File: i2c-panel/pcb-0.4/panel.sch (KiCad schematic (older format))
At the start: 23 parts, among them IC1 ATMEGA168-20PU, P1 CONN_6, P2 I2C, P7 CONN_2, SW1 PUSHPUTTON, SW2 PUSHPUTTON, SW3 PUSHPUTTON, SW4 PUSHPUTTON, SW5 JOYSTICK, T1 BC547C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

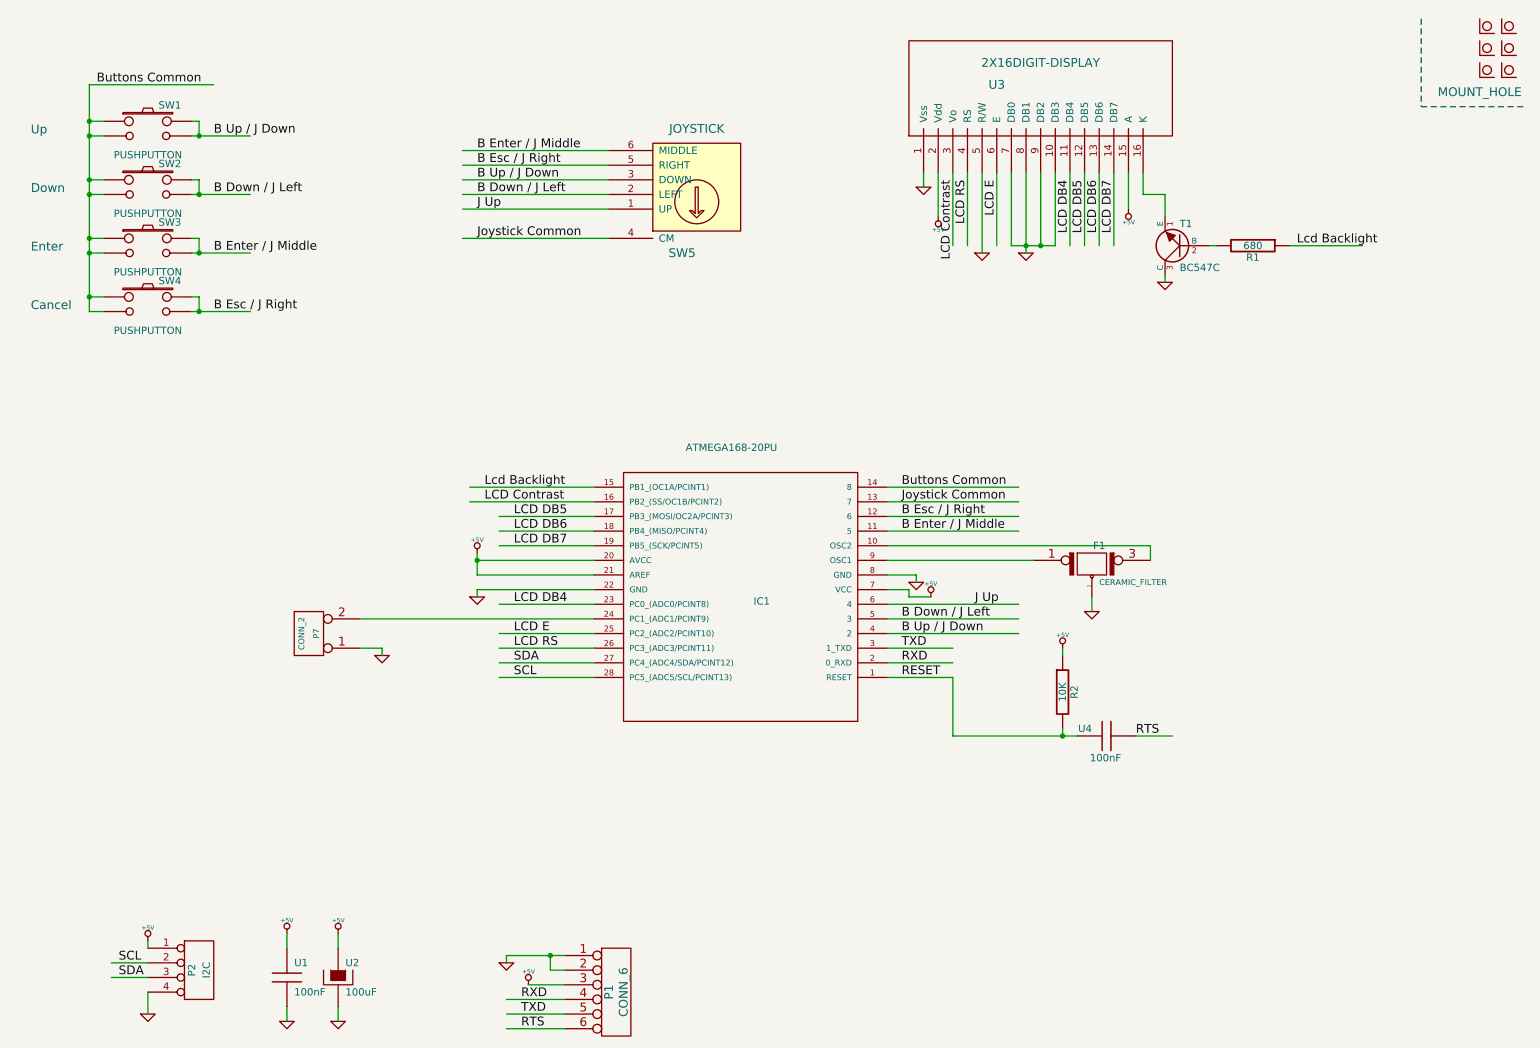
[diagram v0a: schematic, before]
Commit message: I2C level converter, FET for buzzer and ISP connector added
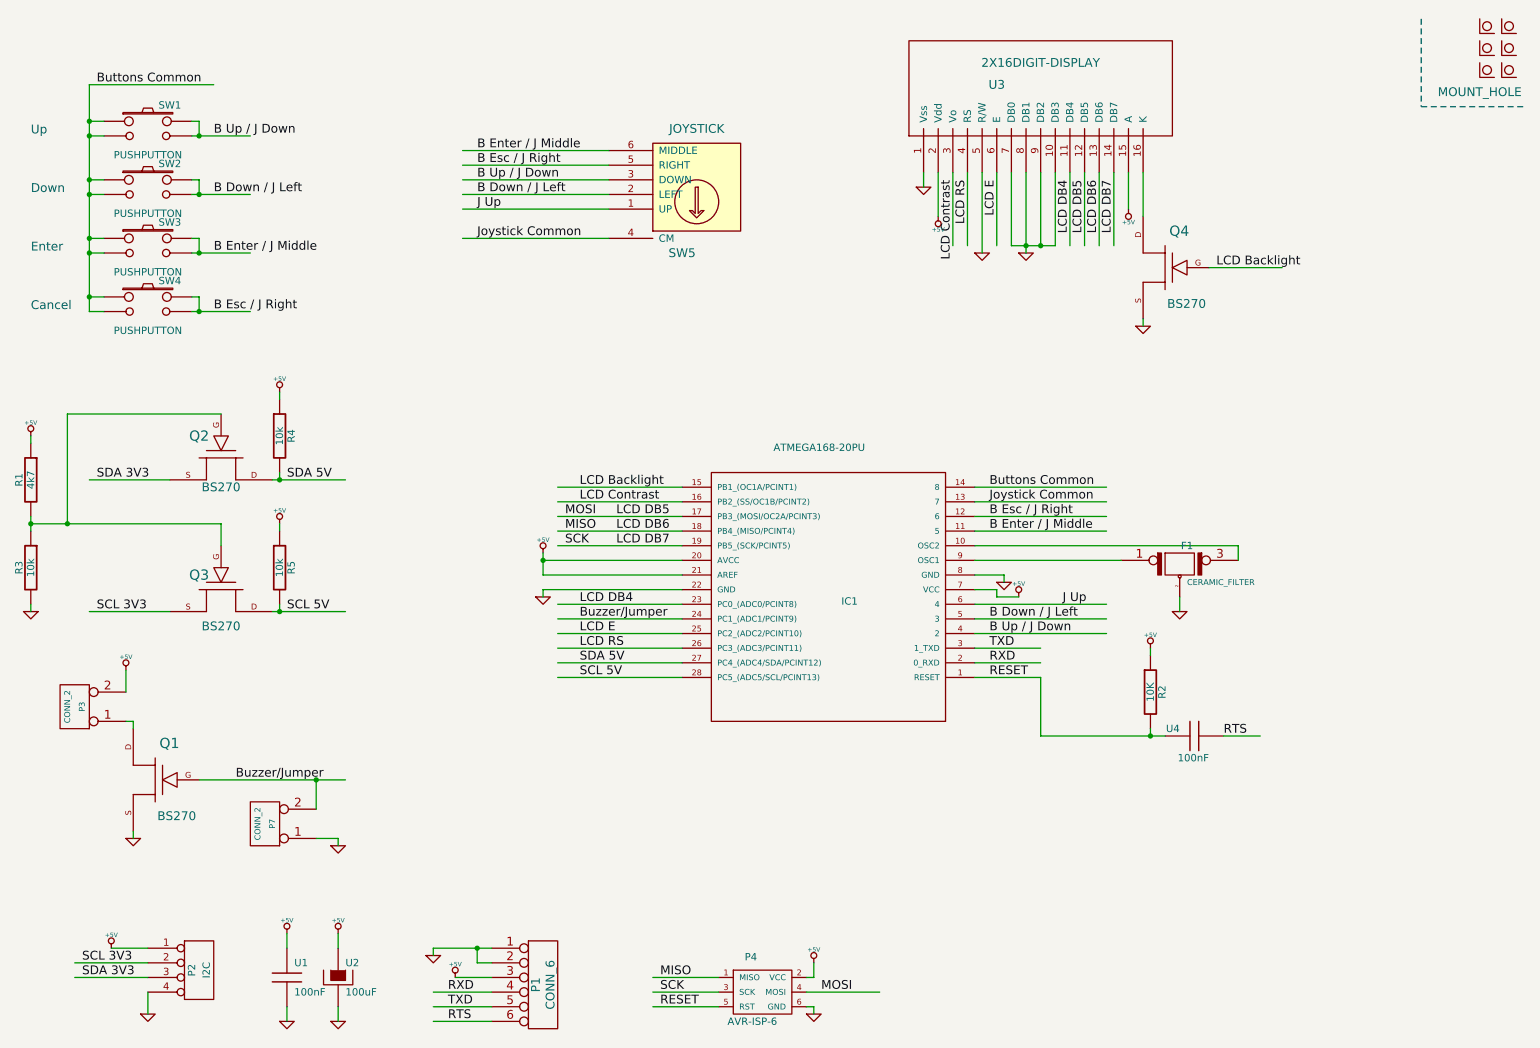
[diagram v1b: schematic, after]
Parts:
- removed T1: BC547C, symbol NPN
- added P3: CONN_2, SIL-1, symbol CONN_2
- added P4: AVR-ISP-6, SIL-1, symbol AVR-ISP-6
- added Q1, Q2, Q3, Q4: BS270, TO92DGS, symbol FET_N
- added R3, R4, R5: 10k, R4, symbol R
- F1: footprint (none) -> SIL-3
- H1, H2, H3, H4, H5, H6: footprint (none) -> HOLE_3MM
- IC1: footprint MLF44 -> DIP-28__300_ELL
- P1: footprint (none) -> SIL-6
- P2: footprint (none) -> SIL-4
- P7: footprint (none) -> SIL-2
- R1: value 680 -> 4k7; footprint (none) -> R4
- R2: footprint (none) -> R4
- SW1, SW2, SW3, SW4: footprint (none) -> PUSHBUTTON
- SW5: footprint (none) -> JOYSTICK_FLIPPED_RIGHT
- U1, U4: footprint (none) -> C2
- U2: footprint (none) -> CCAP_3.5MM
- U3: footprint (none) -> SIL-16
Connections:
- net labels added: Buzzer/Jumper, LCD Backlight, MISO, MOSI, SCK, SCL 3V3, SCL 5V, SDA 3V3, SDA 5V
- net labels removed: Lcd Backlight, SCL, SDA
- wire segments 108 -> 134
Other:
- moved on the sheet: F1, IC1, P1, P7, R2, U4

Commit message: I2C level shifter: not neccesary, pcb enlarged for extra mounting holes
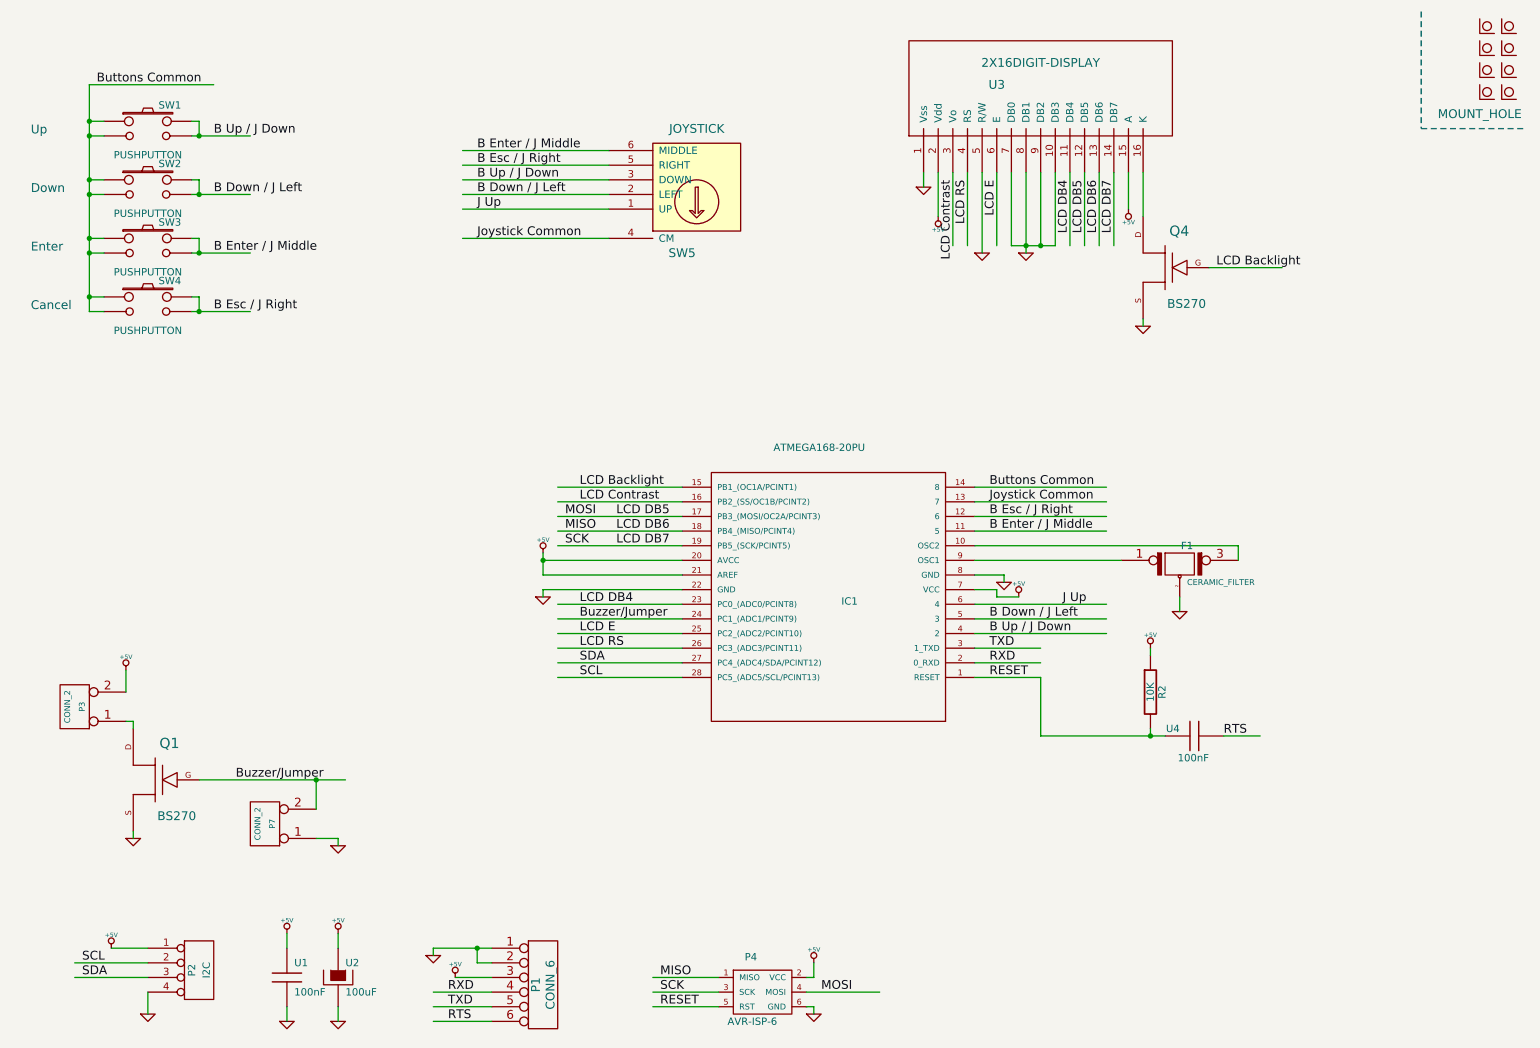
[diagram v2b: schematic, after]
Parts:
- removed Q2, Q3: BS270, TO92DGS, symbol FET_N
- removed R1: 4k7, R4, symbol R
- removed R3, R4, R5: 10k, R4, symbol R
- added H7, H8: MOUNT_HOLE, HOLE_3MM, symbol MOUNT_HOLE
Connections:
- net labels added: SCL, SDA
- net labels removed: SCL 3V3, SCL 5V, SDA 3V3, SDA 5V
- wire segments 134 -> 119

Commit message: Larger holes for pinheaders, extra connector for buzzer
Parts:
- added P5: CONN_4, SIL-4, symbol CONN_4
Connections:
- wire segments 119 -> 124

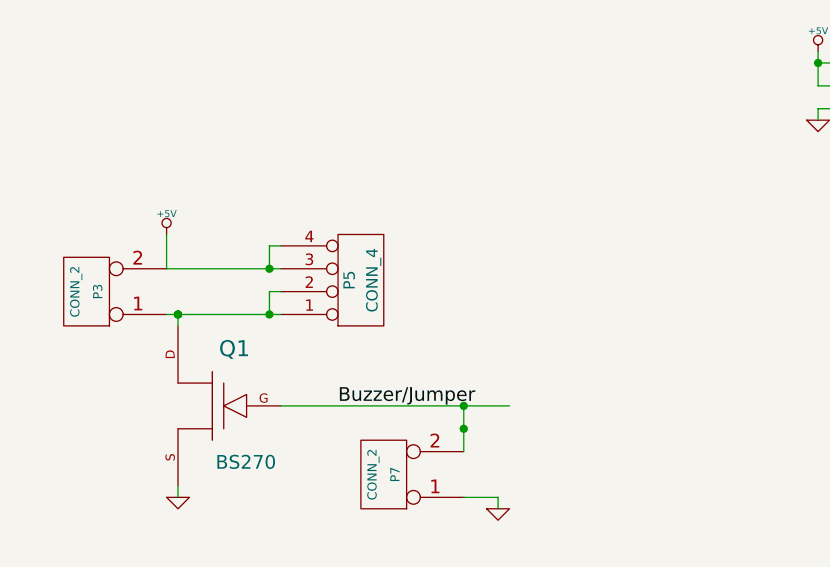
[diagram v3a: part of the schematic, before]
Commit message: Kingstate KPEG242 buzzer
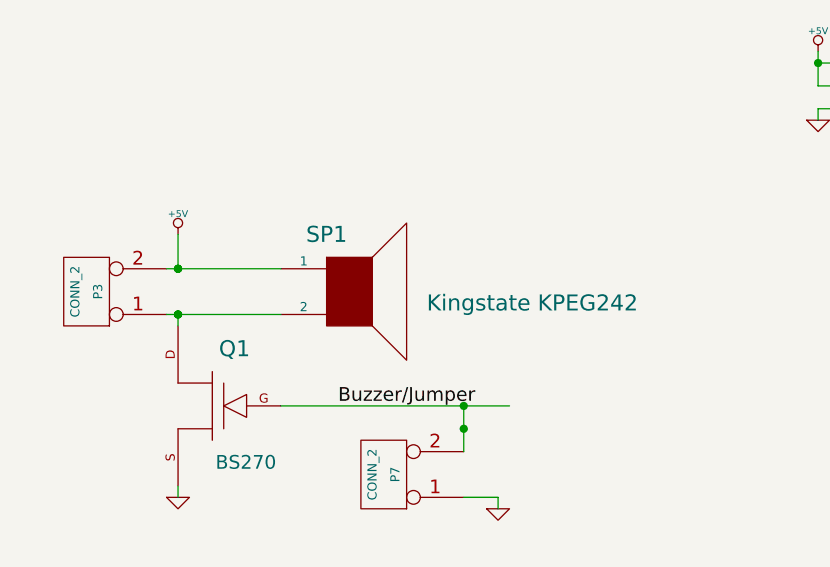
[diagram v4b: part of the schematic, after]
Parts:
- removed P5: CONN_4, SIL-4, symbol CONN_4
- added SP1: Kingstate KPEG242, KPEG242, symbol SPEAKER
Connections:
- wire segments 124 -> 120
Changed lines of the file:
@@
-EESchema Schematic File Version 2  date Wed 17 Apr 2013 20:22:37 CEST
+EESchema Schematic File Version 2  date Wed 17 Apr 2013 21:05:51 CEST
 LIBS:panel-cache
 LIBS:power
@@
 Comment4 ""
 $EndDescr
+$Comp
+L SPEAKER SP1
+U 1 1 516EEF84
+P 2300 5350
+F 0 "SP1" H 2200 5600 70  0000 C CNN
+F 1 "Kingstate KPEG242" H 3100 5300 70  0000 C CNN
+F 2 "KPEG242" H 2300 5350 60  0001 C CNN
+	1    2300 5350
+	1    0    0    -1
+$EndComp
+Connection ~ 1550 5250
+Connection ~ 1550 5250
 Wire Wire Line
 	2800 6250 2950 6250
-Connection ~ 1950 5250
 Wire Wire Line
 	2000 5250 1500 5250
-Wire Wire Line
-	1950 5250 1950 5150
-Connection ~ 1950 5450
-Wire Wire Line
-	1950 5450 1950 5350
-Wire Wire Line
-	1950 5350 2000 5350
 Wire Wire Line
 	2000 5450 1500 5450
@@
 	1550 5500 1550 5450
 Wire Wire Line
-	1500 5250 1500 5100
+	1550 5250 1550 5100
 Wire Wire Line
 	4450 4150 5300 4150
@@
 	8450 2000 8450 1700
 Connection ~ 2800 5950
-Wire Wire Line
-	1950 5150 2000 5150
 Connection ~ 1550 5450
 Connection ~ 1550 5450
-$Comp
-L CONN_4 P5
-U 1 1 516EE28D
-P 2350 5300
-F 0 "P5" V 2300 5300 50  0000 C CNN
-F 1 "CONN_4" V 2400 5300 50  0000 C CNN
-F 2 "SIL-4" H 2350 5300 60  0001 C CNN
-	1    2350 5300
-	1    0    0    1
-$EndComp
 $Comp
 L MOUNT_HOLE H7
@@
 L +5V #PWR03
 U 1 1 514EBB4F
-P 1500 5100
-F 0 "#PWR03" H 1500 5190 20  0001 C CNN
-F 1 "+5V" H 1500 5190 30  0000 C CNN
-	1    1500 5100
-	1    0    0    -1
-$EndComp
+P 1550 5100
+F 0 "#PWR03" H 1550 5190 20  0001 C CNN
+F 1 "+5V" H 1550 5190 30  0000 C CNN
+	1    1550 5100
+	1    0    0    -1
+$EndComp
